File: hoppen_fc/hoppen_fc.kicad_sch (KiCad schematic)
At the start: 0 parts

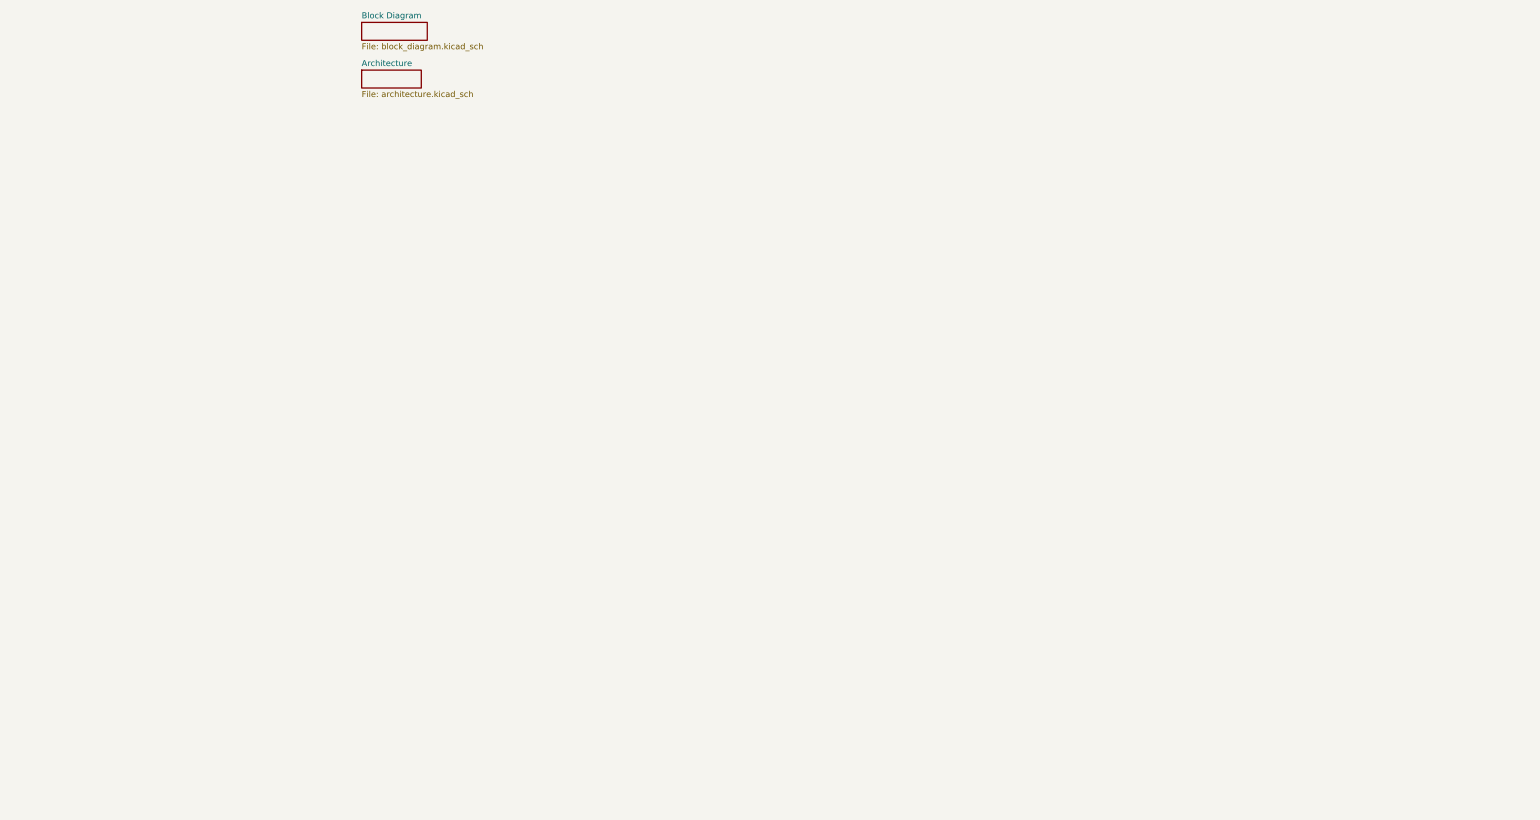
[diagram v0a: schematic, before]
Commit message: finished adding lcsc numbers
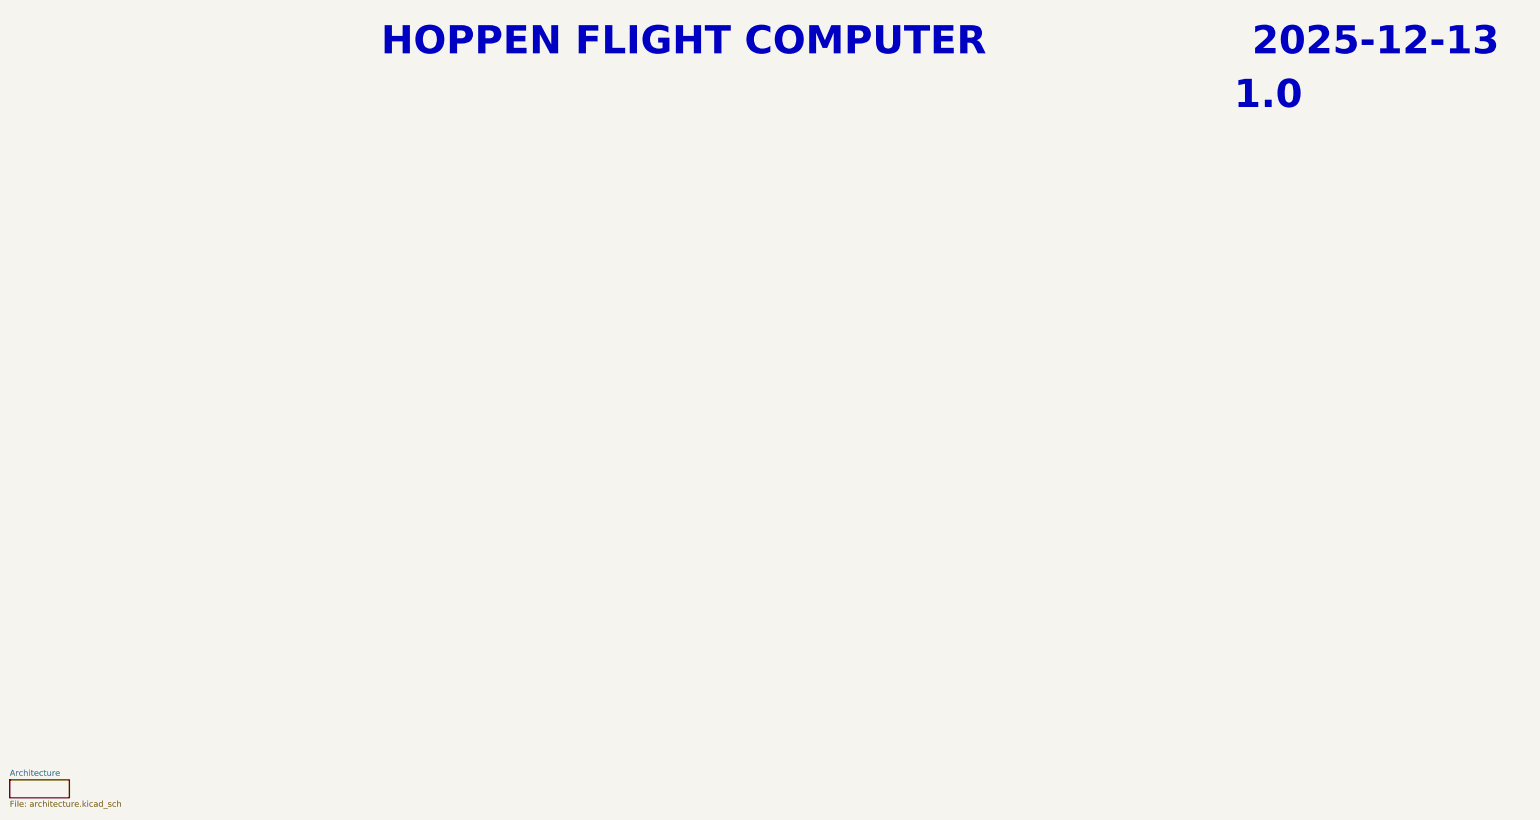
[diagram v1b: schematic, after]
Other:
- removed sheet Block Diagram
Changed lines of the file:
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@@
 		(company "Hoppen")
 	)
-	(sheet
-		(at 17.78 20.32)
-		(size 13.97 3.81)
+	(text_box "${REVISION}"
 		(exclude_from_sim no)
-		(in_bom yes)
-		(on_board yes)
-		(dnp no)
-		(fields_autoplaced yes)
+		(at 161.29 29.21 0)
+		(size 99.06 12.7)
+		(margins 4.4999 4.4999 4.4999 4.4999)
 		(stroke
-			(width 0.1524)
+			(width -0.0001)
 			(type solid)
 		)
 		(fill
-			(color 0 0 0 0.0000)
+			(type none)
 		)
-		(property "Sheetname" "Block Diagram"
-			(at 17.78 19.6084 0)
-			(effects
-				(font
-					(size 1.27 1.27)
-				)
-				(justify left bottom)
+		(effects
+			(font
+				(face "KiCad Font")
+				(size 6 6)
+				(thickness 1.2)
+				(bold yes)
 			)
 		)
-		(property "Sheetfile" "block_diagram.kicad_sch"
-			(at 17.78 24.7146 0)
-			(effects
-				(font
-					(size 1.27 1.27)
-				)
-				(justify left top)
+	)
+	(text_box "HOPPEN FLIGHT COMPUTER"
+		(exclude_from_sim no)
+		(at 16.51 17.78 0)
+		(size 139.7 12.7)
+		(margins 4.4999 4.4999 4.4999 4.4999)
+		(stroke
+			(width -0.0001)
+			(type solid)
+		)
+		(fill
+			(type none)
+		)
+		(effects
+			(font
+				(face "KiCad Font")
+				(size 6 6)
+				(thickness 1.2)
+				(bold yes)
 			)
 		)
-		(instances
-			(project "hoppen_fc"
-				(path "/abe950a1-9eef-4508-9fd4-31d3e723e029"
-					(page "2")
-				)
+	)
+	(text_box "${ISSUE_DATE}"
+		(exclude_from_sim no)
+		(at 184.15 17.78 0)
+		(size 99.06 12.7)
+		(margins 4.4999 4.4999 4.4999 4.4999)
+		(stroke
+			(width -0.0001)
+			(type solid)
+		)
+		(fill
+			(type none)
+		)
+		(effects
+			(font
+				(face "KiCad Font")
+				(size 6 6)
+				(thickness 1.2)
+				(bold yes)
 			)
 		)
 	)
 	(sheet
-		(at 17.78 30.48)
+		(at -57.15 181.61)
 		(size 12.7 3.81)
 		(exclude_from_sim no)
@@
 		)
 		(property "Sheetname" "Architecture"
-			(at 17.78 29.7684 0)
+			(at -57.15 180.8984 0)
 			(effects
 				(font
@@
 		)
 		(property "Sheetfile" "architecture.kicad_sch"
-			(at 17.78 34.8746 0)
+			(at -57.15 186.0046 0)
 			(effects
 				(font
